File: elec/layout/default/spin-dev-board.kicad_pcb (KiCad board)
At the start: 2 copper layers, 225.7 x 100.8 mm, 30 parts

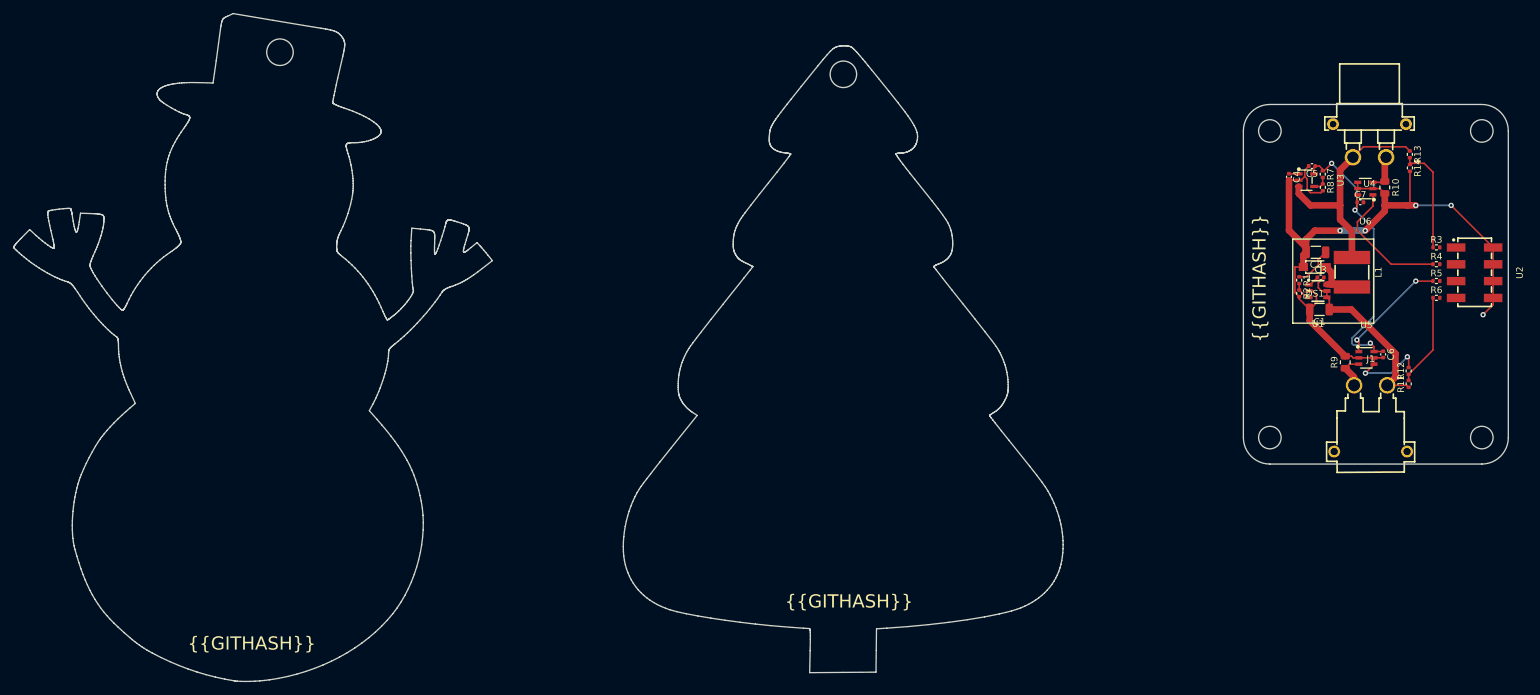
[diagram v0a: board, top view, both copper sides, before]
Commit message: deleting unused layouts
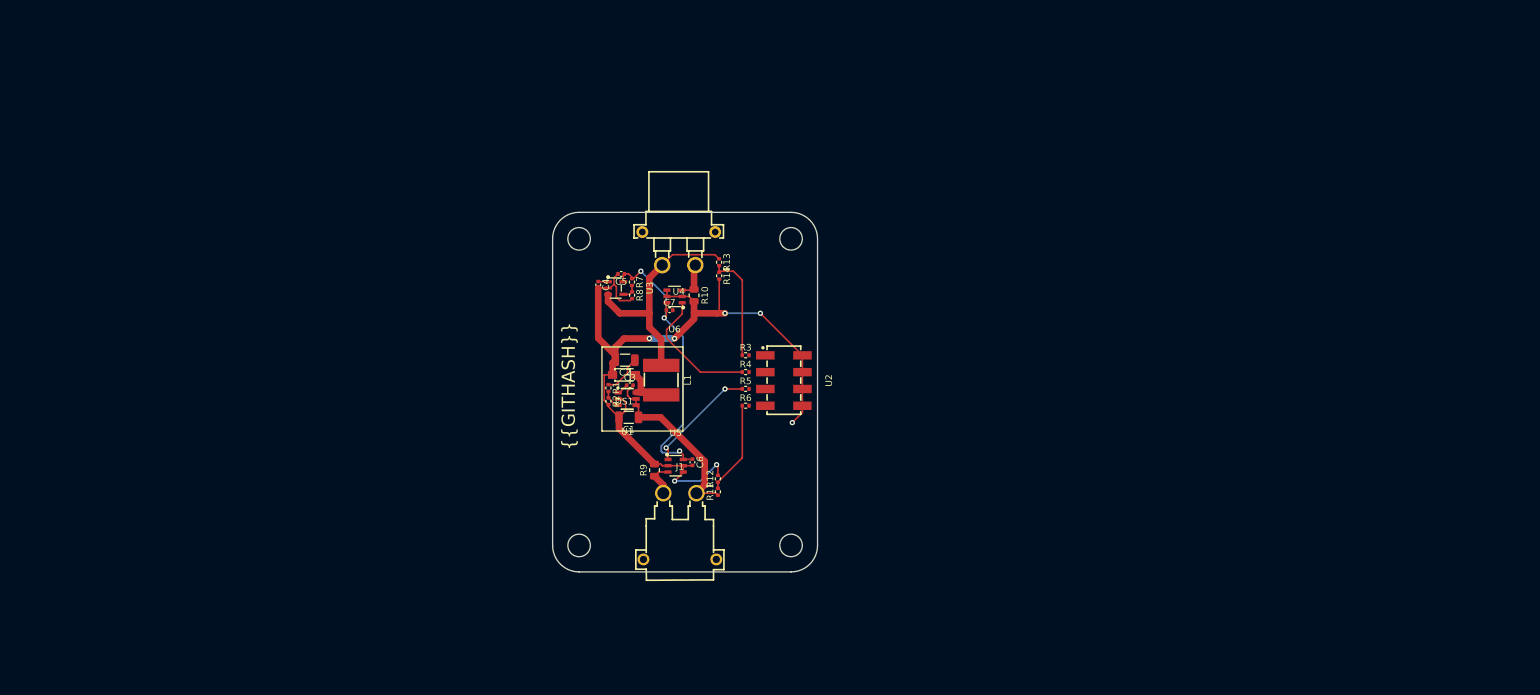
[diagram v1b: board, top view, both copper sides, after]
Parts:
- moved U2 105.6 mm to (152.2, 105.2)
- moved C4 105.6 mm to (124.2, 90.7)
- moved C1 105.6 mm to (128.8, 110.7)
- moved C2 105.6 mm to (128.3, 102.1)
- moved C3 105.6 mm to (129.0, 105.9)
- moved C6 105.6 mm to (138.4, 117.5)
- moved C7 105.6 mm to (135.0, 94.6)
- moved DS1 105.6 mm to (128.1, 104.3)
- moved J1 105.6 mm to (136.5, 127.2)
- moved L1 105.6 mm to (133.7, 105.1)
- moved R10 105.6 mm to (138.7, 92.3)
- moved R11 105.6 mm to (142.3, 122.0)
- moved R12 105.6 mm to (142.3, 120.0)
- moved R13 105.6 mm to (142.5, 87.3)
- moved R14 105.6 mm to (142.5, 89.4)
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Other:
- board size 225.7 x 100.8 mm -> 40 x 54.3 mm

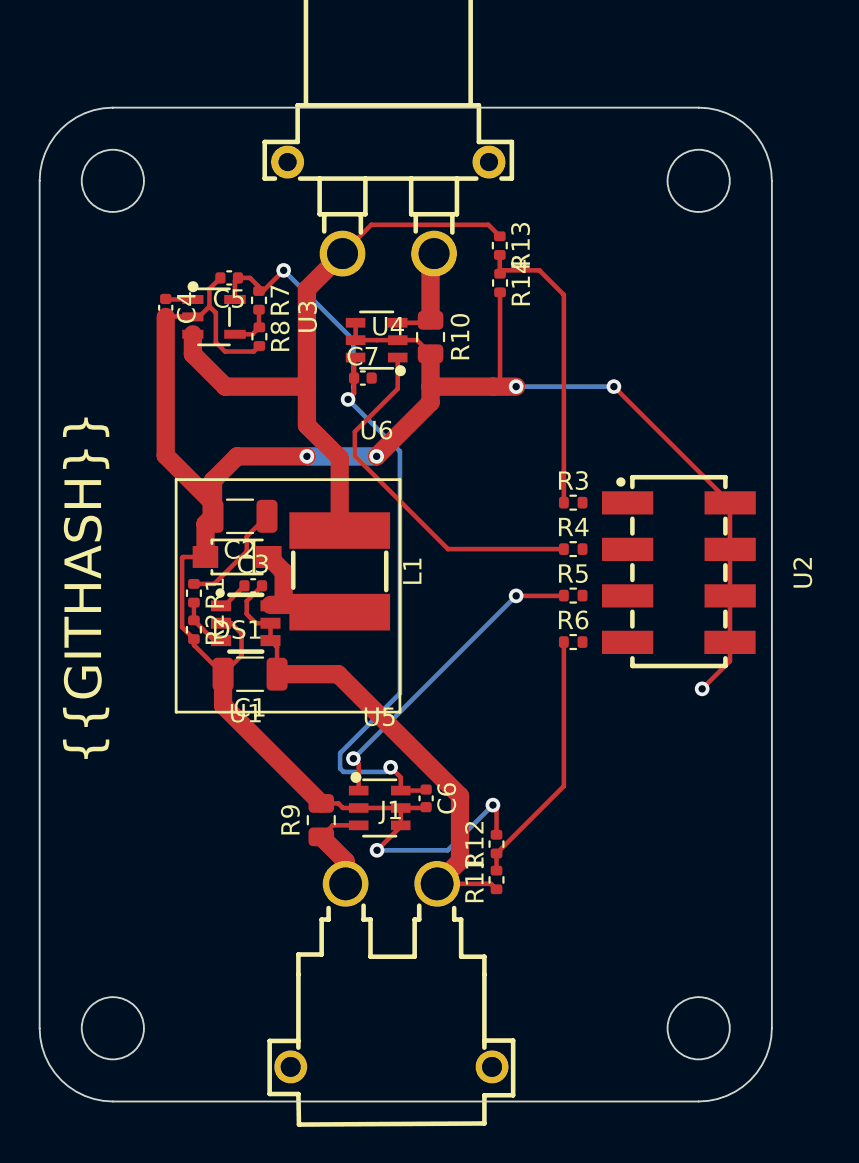
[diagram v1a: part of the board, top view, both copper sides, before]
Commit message: cleanup silk screen
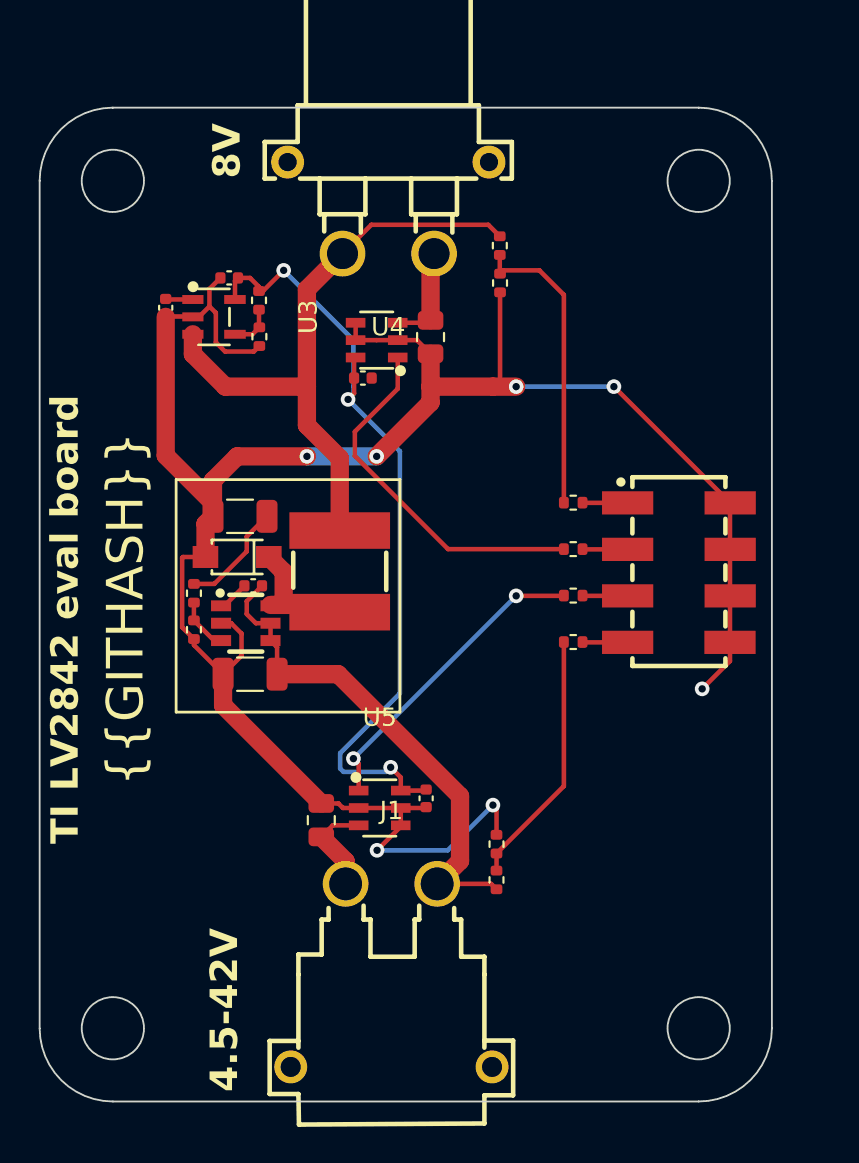
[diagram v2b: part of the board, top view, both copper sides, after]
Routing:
- net _7: track 0.00 -> 2.47 mm
- net _5: track 0.00 -> 2.47 mm
- net _3: track 0.00 -> 2.47 mm
- net _1: track 0.00 -> 2.47 mm
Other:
- board text added: "4.5-42V"
- board text added: "8V"
- board text added: "TI LV2842 eval board"
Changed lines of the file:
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@@
     (tags "capacitor")
     (attr smd)
-    (fp_text reference "C2" (at 0 -1.85 180) (layer "F.SilkS")
+    (fp_text reference "C2" (at 0 -1.85 180) (layer "F.SilkS") hide
         (effects (font (size 1 1) (thickness 0.15)))
     )
@@
     (tags "resistor")
     (attr smd)
-    (fp_text reference "R12" (at 0 -1.17 90) (layer "F.SilkS")
+    (fp_text reference "R12" (at 0 -1.17 90) (layer "F.SilkS") hide
         (effects (font (size 1 1) (thickness 0.15)))
     )
@@
     (tags "resistor")
     (attr smd)
-    (fp_text reference "R14" (at 0 -1.17 -90) (layer "F.SilkS")
+    (fp_text reference "R14" (at 0 -1.17 -90) (layer "F.SilkS") hide
         (effects (font (size 1 1) (thickness 0.15)))
     )
@@
     (tags "resistor")
     (attr smd)
-    (fp_text reference "R13" (at 0 -1.17 -90) (layer "F.SilkS")
+    (fp_text reference "R13" (at 0 -1.17 -90) (layer "F.SilkS") hide
         (effects (font (size 1 1) (thickness 0.15)))
     )
@@
     (tags "capacitor")
     (attr smd)
-    (fp_text reference "C3" (at 0 -1.16) (layer "F.SilkS")
+    (fp_text reference "C3" (at 0 -1.16) (layer "F.SilkS") hide
         (effects (font (size 1 1) (thickness 0.15)))
     )
@@
     (at 152.249002 105.186682 -90)
     (attr smd)
-    (fp_text reference "U2" (at 0 -6.8 -90) (layer "F.SilkS")
+    (fp_text reference "U2" (at 0 -6.8 -90) (layer "F.SilkS") hide
         (effects (font (size 1 1) (thickness 0.15)))
     )
@@
     (tags "capacitor")
     (attr smd)
-    (fp_text reference "C5" (at 0 -1.16 180) (layer "F.SilkS")
+    (fp_text reference "C5" (at 0 -1.16 180) (layer "F.SilkS") hide
         (effects (font (size 1 1) (thickness 0.15)))
     )
@@
     (tags "resistor")
     (attr smd)
-    (fp_text reference "R4" (at 0 -1.17) (layer "F.SilkS")
+    (fp_text reference "R4" (at 0 -1.17) (layer "F.SilkS") hide
         (effects (font (size 1 1) (thickness 0.15)))
     )
@@
     (at 133.721361 105.118639 -90)
     (attr smd)
-    (fp_text reference "L1" (at 0 -4 -90) (layer "F.SilkS")
+    (fp_text reference "L1" (at 0 -4 -90) (layer "F.SilkS") hide
         (effects (font (size 1 1) (thickness 0.15)))
     )
@@
     (tags "capacitor")
     (attr smd)
-    (fp_text reference "C1" (at 0 -1.85 180) (layer "F.SilkS")
+    (fp_text reference "C1" (at 0 -1.85 180) (layer "F.SilkS") hide
         (effects (font (size 1 1) (thickness 0.15)))
     )
@@
     (tags "resistor")
     (attr smd)
-    (fp_text reference "R11" (at 0 -1.17 90) (layer "F.SilkS")
+    (fp_text reference "R11" (at 0 -1.17 90) (layer "F.SilkS") hide
         (effects (font (size 1 1) (thickness 0.15)))
     )
@@
     (tags "resistor")
     (attr smd)
-    (fp_text reference "R8" (at 0 -1.17 -90) (layer "F.SilkS")
+    (fp_text reference "R8" (at 0 -1.17 -90) (layer "F.SilkS") hide
         (effects (font (size 1 1) (thickness 0.15)))
     )
@@
     (at 135.739002 92.486682 180)
     (attr smd)
-    (fp_text reference "U6" (at 0 -4.95 180) (layer "F.SilkS")
+    (fp_text reference "U6" (at 0 -4.95 180) (layer "F.SilkS") hide
         (effects (font (size 1 1) (thickness 0.15)))
     )
@@
     (at 128.118104 104.33261 180)
     (attr smd)
-    (fp_text reference "DS1" (at 0 -4 180) (layer "F.SilkS")
+    (fp_text reference "DS1" (at 0 -4 180) (layer "F.SilkS") hide
         (effects (font (size 1 1) (thickness 0.15)))
     )
@@
     (at 128.59 107.95 180)
     (attr smd)
-    (fp_text reference "U1" (at 0 -4.95 180) (layer "F.SilkS")
+    (fp_text reference "U1" (at 0 -4.95 180) (layer "F.SilkS") hide
         (effects (font (size 1 1) (thickness 0.15)))
     )
@@
     (tags "capacitor")
     (attr smd)
-    (fp_text reference "C4" (at 0 -1.16 -90) (layer "F.SilkS")
+    (fp_text reference "C4" (at 0 -1.16 -90) (layer "F.SilkS") hide
         (effects (font (size 1 1) (thickness 0.15)))
     )
@@
     (tags "capacitor")
     (attr smd)
-    (fp_text reference "C6" (at 0 -1.16 -90) (layer "F.SilkS")
+    (fp_text reference "C6" (at 0 -1.16 -90) (layer "F.SilkS") hide
         (effects (font (size 1 1) (thickness 0.15)))
     )
@@
     (tags "resistor")
     (attr smd)
-    (fp_text reference "R1" (at 0 -1.17 -90) (layer "F.SilkS")
+    (fp_text reference "R1" (at 0 -1.17 -90) (layer "F.SilkS") hide
         (effects (font (size 1 1) (thickness 0.15)))
     )
@@
     (tags "resistor")
     (attr smd)
-    (fp_text reference "R9" (at 0 -1.65 90) (layer "F.SilkS")
+    (fp_text reference "R9" (at 0 -1.65 90) (layer "F.SilkS") hide
         (effects (font (size 1 1) (thickness 0.15)))
     )
@@
     (tags "resistor")
     (attr smd)
-    (fp_text reference "R3" (at 0 -1.17) (layer "F.SilkS")
+    (fp_text reference "R3" (at 0 -1.17) (layer "F.SilkS") hide
         (effects (font (size 1 1) (thickness 0.15)))
     )
@@
     (tags "capacitor")
     (attr smd)
-    (fp_text reference "C7" (at 0 -1.16) (layer "F.SilkS")
+    (fp_text reference "C7" (at 0 -1.16) (layer "F.SilkS") hide
         (effects (font (size 1 1) (thickness 0.15)))
     )
@@
     (tags "resistor")
     (attr smd)
-    (fp_text reference "R7" (at 0 -1.17 -90) (layer "F.SilkS")
+    (fp_text reference "R7" (at 0 -1.17 -90) (layer "F.SilkS") hide
         (effects (font (size 1 1) (thickness 0.15)))
     )
@@
     (tags "resistor")
     (attr smd)
-    (fp_text reference "R5" (at 0 -1.17) (layer "F.SilkS")
+    (fp_text reference "R5" (at 0 -1.17) (layer "F.SilkS") hide
         (effects (font (size 1 1) (thickness 0.15)))
     )
@@
     (tags "resistor")
     (attr smd)
-    (fp_text reference "R10" (at 0 -1.65 -90) (layer "F.SilkS")
+    (fp_text reference "R10" (at 0 -1.65 -90) (layer "F.SilkS") hide
         (effects (font (size 1 1) (thickness 0.15)))
     )
@@
     (tags "resistor")
     (attr smd)
-    (fp_text reference "R6" (at 0 -1.17) (layer "F.SilkS")
+    (fp_text reference "R6" (at 0 -1.17) (layer "F.SilkS") hide
         (effects (font (size 1 1) (thickness 0.15)))
     )
@@
     (tags "resistor")
     (attr smd)
-    (fp_text reference "R2" (at 0 -1.17 -90) (layer "F.SilkS")
+    (fp_text reference "R2" (at 0 -1.17 -90) (layer "F.SilkS") hide
         (effects (font (size 1 1) (thickness 0.15)))
     )
@@
   (gr_line (start 121.329002 134.076682) (end 153.329002 134.076682)
     (stroke (width 0.1) (type solid)) (layer "Edge.Cuts"))
-  (gr_text "{{GITHASH}}" (at 120.930637 115.707681 90) (layer "F.SilkS")
+  (gr_text "4.5-42V" (at 128.294906 133.55667 90) (layer "F.SilkS")
+    (effects (font (size 1.5 1.5) (thickness 0.3) bold) (justify left bottom))
+  )
+  (gr_text "TI LV2842 eval board" (at 119.593142 120.006955 90) (layer "F.SilkS")
+    (effects (font (size 1.5 1.5) (thickness 0.3) bold) (justify left bottom))
+  )
+  (gr_text "{{GITHASH}}" (at 123.19 116.84 90) (layer "F.SilkS")
     (effects (font (size 2 2) (thickness 0.1)) (justify left bottom))
+  )
+  (gr_text "8V" (at 128.43511 83.656461 90) (layer "F.SilkS")
+    (effects (font (size 1.5 1.5) (thickness 0.3) bold) (justify left bottom))
   )
   (segment (start 128.119002 98.836682) (end 131.929002 98.836682) (width 1) (layer "F.Cu") (net 1))
@@
   (segment (start 144.629002 88.676682) (end 142.657909 88.676682) (width 0.25) (layer "F.Cu") (net 12))
   (segment (start 142.465672 88.843293) (end 142.478485 88.856106) (width 0.25) (layer "F.Cu") (net 12))
+  (segment (start 146.997161 101.376682) (end 146.985843 101.365364) (width 0.25) (layer "F.Cu") (net 13))
+  (segment (start 149.449002 101.376682) (end 146.997161 101.376682) (width 0.25) (layer "F.Cu") (net 13))
   (segment (start 134.546361 97.489323) (end 134.546361 98.810767) (width 0.25) (layer "F.Cu") (net 14))
   (segment (start 136.889002 93.436682) (end 136.889002 95.146682) (width 0.25) (layer "F.Cu") (net 14))
@@
   (segment (start 139.638687 103.903093) (end 145.965843 103.903093) (width 0.25) (layer "F.Cu") (net 14))
   (segment (start 134.546361 98.810767) (end 139.638687 103.903093) (width 0.25) (layer "F.Cu") (net 14))
+  (segment (start 149.449002 103.916682) (end 146.999432 103.916682) (width 0.25) (layer "F.Cu") (net 15))
+  (segment (start 146.999432 103.916682) (end 146.985843 103.903093) (width 0.25) (layer "F.Cu") (net 15))
+  (segment (start 147.001703 106.456682) (end 146.985843 106.440822) (width 0.25) (layer "F.Cu") (net 16))
+  (segment (start 149.449002 106.456682) (end 147.001703 106.456682) (width 0.25) (layer "F.Cu") (net 16))
+  (segment (start 149.449002 108.996682) (end 147.003974 108.996682) (width 0.25) (layer "F.Cu") (net 17))
+  (segment (start 147.003974 108.996682) (end 146.985843 108.978551) (width 0.25) (layer "F.Cu") (net 17))
   (segment (start 128.952518 92.166682) (end 129.33152 91.78768) (width 0.25) (layer "F.Cu") (net 18))
   (segment (start 127.999002 92.166682) (end 128.952518 92.166682) (width 0.25) (layer "F.Cu") (net 18))

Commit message: drc fixes
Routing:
- net vcc-1: track 41.7 -> 52.8 mm, vias 0 -> 2
- net gnd: track 121.5 -> 123.6 mm
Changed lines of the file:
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@@
   (segment (start 126.604002 89.688234) (end 126.604002 90.646682) (width 0.25) (layer "F.Cu") (net 1))
   (segment (start 137.938947 92.486682) (end 138.683086 93.230821) (width 0.25) (layer "F.Cu") (net 1))
+  (segment (start 135.739002 94.285022) (end 135.739002 92.486682) (width 0.25) (layer "F.Cu") (net 1))
   (segment (start 148.439002 95.026682) (end 148.699002 95.026682) (width 0.25) (layer "F.Cu") (net 1))
   (segment (start 155.039002 108.996682) (end 155.039002 101.386682) (width 0.25) (layer "F.Cu") (net 1))
@@
   (segment (start 126.604002 90.646682) (end 126.034002 91.216682) (width 0.25) (layer "F.Cu") (net 1))
   (segment (start 125.677963 91.195643) (end 125.699002 91.216682) (width 0.25) (layer "F.Cu") (net 1))
+  (segment (start 135.465481 94.558543) (end 135.739002 94.285022) (width 0.25) (layer "F.Cu") (net 1))
   (segment (start 134.589002 91.536682) (end 134.589002 92.486682) (width 0.25) (layer "F.Cu") (net 1))
   (via (at 148.699002 95.026682) (size 0.8) (drill 0.4) (layers "F.Cu" "B.Cu") (net 1))
@@
   (segment (start 131.929002 97.139626) (end 131.929002 95.026682) (width 1) (layer "F.Cu") (net 3))
   (segment (start 125.699002 92.166682) (end 125.699002 93.253166) (width 1) (layer "F.Cu") (net 3))
+  (segment (start 131.221044 102.325139) (end 129.963602 102.325139) (width 1) (layer "F.Cu") (net 3))
   (segment (start 128.641361 104.029353) (end 128.641361 103.218248) (width 0.25) (layer "F.Cu") (net 3))
   (segment (start 124.246375 90.266682) (end 124.215336 90.235643) (width 0.25) (layer "F.Cu") (net 3))
   (segment (start 133.721361 102.888639) (end 133.721361 98.931985) (width 1) (layer "F.Cu") (net 3))
   (segment (start 125.757266 105.802903) (end 126.867811 105.802903) (width 0.25) (layer "F.Cu") (net 3))
+  (segment (start 133.721361 102.888639) (end 131.784544 102.888639) (width 1) (layer "F.Cu") (net 3))
   (segment (start 125.699002 90.266682) (end 124.246375 90.266682) (width 0.25) (layer "F.Cu") (net 3))
+  (segment (start 129.963602 102.325139) (end 129.749036 102.110573) (width 1) (layer "F.Cu") (net 3))
+  (segment (start 125.699002 90.266682) (end 125.699002 88.811656) (width 0.25) (layer "F.Cu") (net 3))
   (segment (start 133.721361 98.931985) (end 131.929002 97.139626) (width 1) (layer "F.Cu") (net 3))
   (segment (start 142.465672 86.812705) (end 141.838325 86.185358) (width 0.25) (layer "F.Cu") (net 3))
+  (segment (start 125.699002 88.811656) (end 125.38527 88.497924) (width 0.25) (layer "F.Cu") (net 3))
   (segment (start 127.472518 95.026682) (end 131.929002 95.026682) (width 1) (layer "F.Cu") (net 3))
   (segment (start 141.838325 86.185358) (end 135.448999 86.185358) (width 0.25) (layer "F.Cu") (net 3))
+  (segment (start 131.784544 102.888639) (end 131.221044 102.325139) (width 1) (layer "F.Cu") (net 3))
   (segment (start 126.867811 105.802903) (end 128.641361 104.029353) (width 0.25) (layer "F.Cu") (net 3))
   (segment (start 131.929002 95.026682) (end 131.929002 89.705355) (width 1) (layer "F.Cu") (net 3))
@@
   (segment (start 131.929002 89.705355) (end 133.873999 87.760358) (width 1) (layer "F.Cu") (net 3))
   (segment (start 125.699002 93.253166) (end 127.472518 95.026682) (width 1) (layer "F.Cu") (net 3))
+  (via (at 125.699002 93.253166) (size 0.8) (drill 0.4) (layers "F.Cu" "B.Cu") (net 3))
+  (via (at 125.38527 88.497924) (size 0.8) (drill 0.4) (layers "F.Cu" "B.Cu") (net 3))
+  (segment (start 125.699002 88.811656) (end 125.699002 93.253166) (width 0.25) (layer "B.Cu") (net 3))
+  (segment (start 125.38527 88.497924) (end 125.699002 88.811656) (width 0.25) (layer "B.Cu") (net 3))
   (segment (start 139.043694 122.187873) (end 140.293693 120.937874) (width 1) (layer "F.Cu") (net 4))
   (segment (start 128.641361 107.451361) (end 128.641361 106.74704) (width 0.25) (layer "F.Cu") (net 4))
